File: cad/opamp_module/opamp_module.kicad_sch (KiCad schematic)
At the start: 28 parts, among them J1 Conn_02x04_Odd_Even, U1 OPA2325, U2 REF3433IDBVR

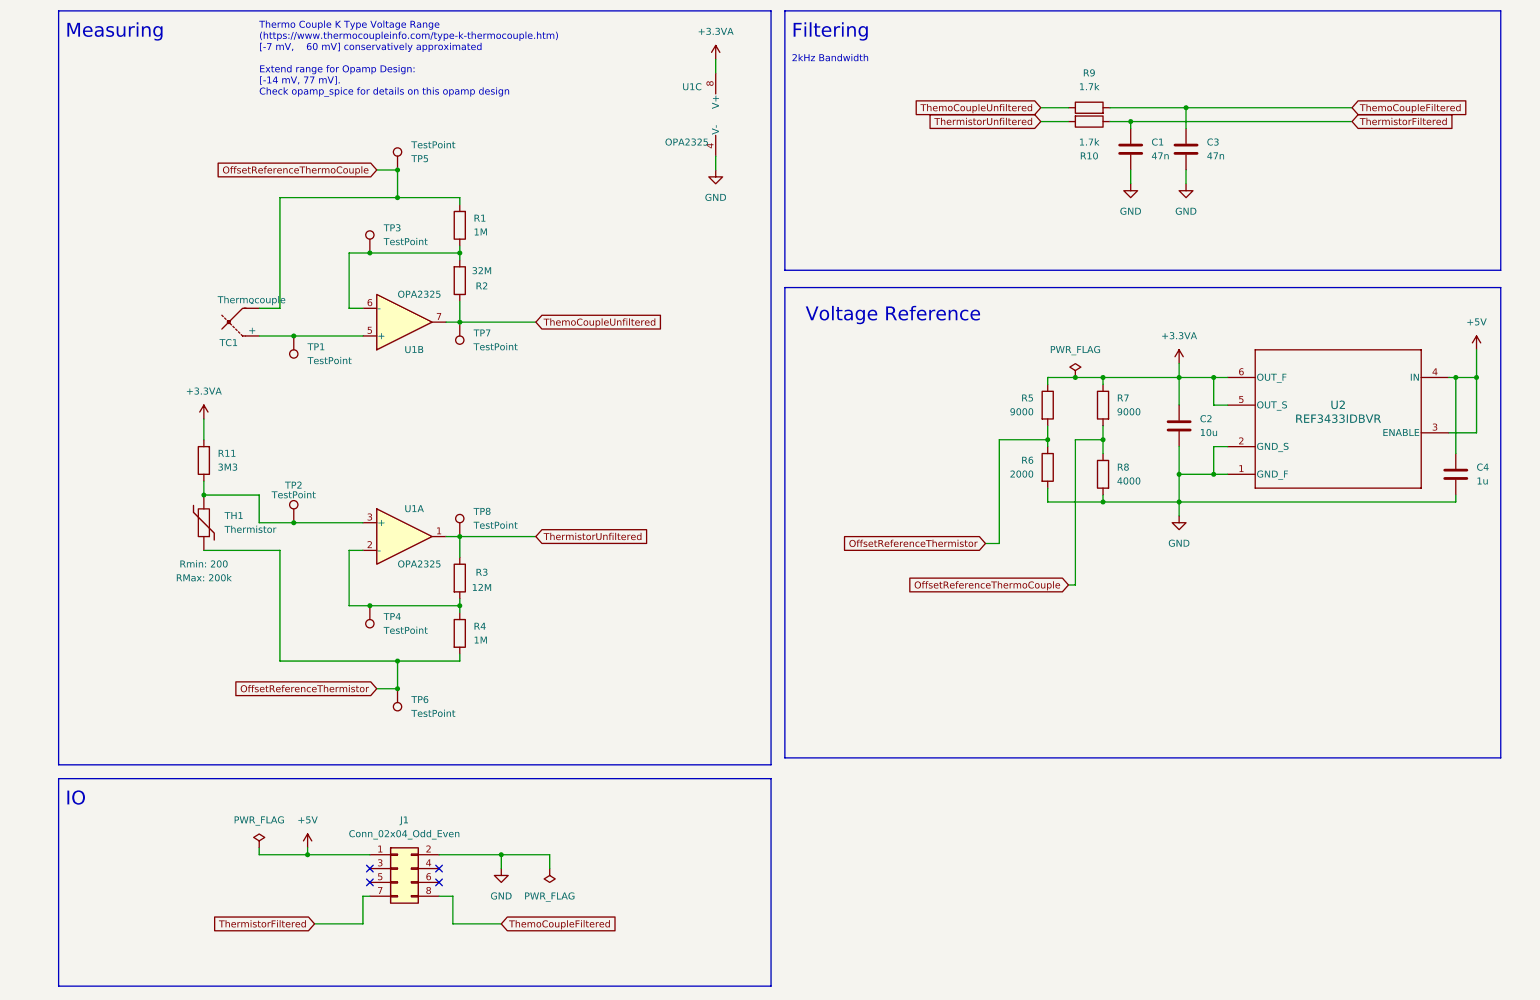
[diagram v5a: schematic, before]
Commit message: Spice simulations and switching to two TC's per module
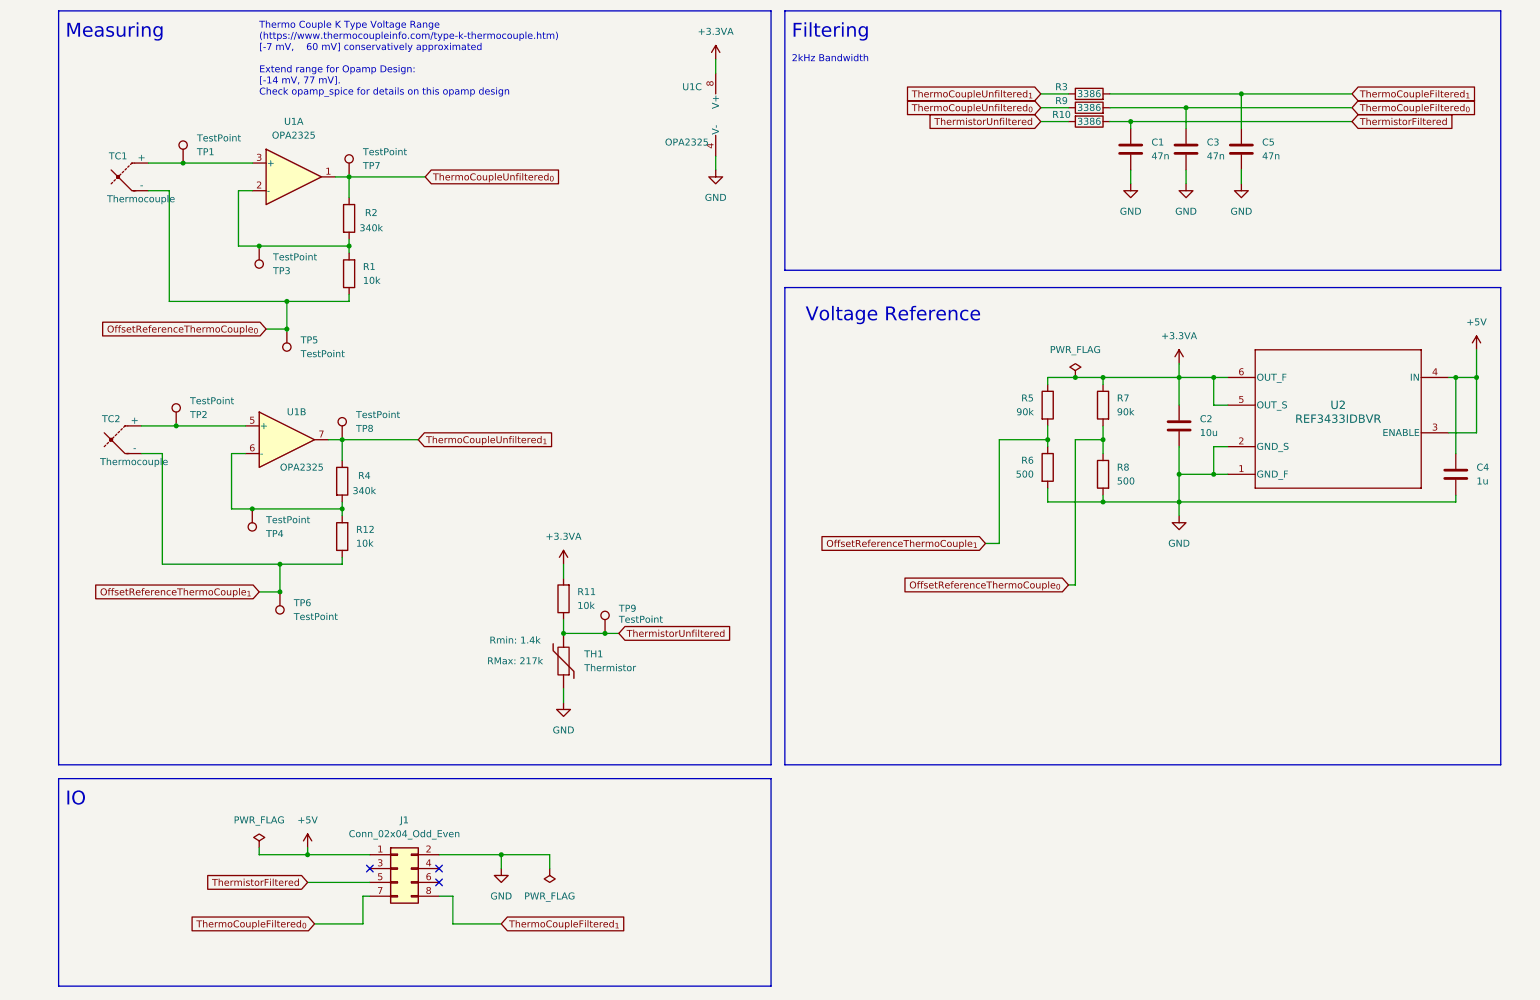
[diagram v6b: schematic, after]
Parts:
- added C5: 47n, Capacitor_SMD:C_0805_2012Metric_Pad1.18x1.45mm_HandSolder, symbol Device:C
- added R12: 10k, Resistor_SMD:R_0805_2012Metric_Pad1.20x1.40mm_HandSolder, symbol Device:R
- added TC2: Thermocouple, Connector_PinHeader_2.54mm:PinHeader_1x02_P2.54mm_Vertical, symbol Device:Thermocouple
- added TP9: TestPoint, TestPoint:TestPoint_Pad_D2.0mm, symbol Connector:TestPoint
- R1: value 1M -> 10k
- R10, R9: value 1.7k -> 3386
- R11: value 3M3 -> 10k
- R2: value 32M -> 340k
- R3: value 12M -> 3386
- R4: value 1M -> 340k
- R5, R7: value 9000 -> 90k
- R6: value 2000 -> 500
- R8: value 4000 -> 500
- TH1: RMax 200k -> 217k; Rmin 200 -> 1.4k
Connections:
- net GND: now also TH1.1, C5.2
- net ThermistorFiltered: now also J1.5 (Pin_5); no longer J1.7 (Pin_7)
- net ThermistorUnfiltered: now also R11.1, TH1.2, TP9.1; no longer R3.1, TP8.1, U1.1
- net at TC1.1 (+), TP1.1: now also U1.3 (+); no longer U1.5 (+)
- net at R2.2, TP3.1: now also R1.2, U1.2 (-); no longer R1.1, U1.6 (-)
- net OffsetReferenceThermistor renamed OffsetReferenceThermoCouple_{1}
- net OffsetReferenceThermoCouple_{1}: now also R12.1, TC2.2 (-); no longer R4.2, TH1.1
- net OffsetReferenceThermoCouple renamed OffsetReferenceThermoCouple_{0}
- net OffsetReferenceThermoCouple_{0}: now also R1.1; no longer R1.2
- net ThemoCoupleFiltered renamed ThermoCoupleFiltered_{0}
- net ThermoCoupleFiltered_{0}: now also J1.7 (Pin_7); no longer J1.8 (Pin_8)
- net ThemoCoupleUnfiltered renamed ThermoCoupleUnfiltered_{0}
- net ThermoCoupleUnfiltered_{0}: now also U1.1; no longer U1.7
- new net: R12.2, R4.2, TP4.1, U1.6 (-)
- new net: TC2.1 (+), TP2.1, U1.5 (+)
- new net ThermoCoupleFiltered_{1}: C5.1, J1.8 (Pin_8), R3.2
- new net ThermoCoupleUnfiltered_{1}: R3.1, R4.1, TP8.1, U1.7
- no-connect marks 4 -> 3
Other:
- moved on the sheet: R1, R11, R2, TC1, TH1, TP1, TP3, TP5, TP7, U1B

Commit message: Ordered
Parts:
- R10, R3, R9: value 3386 -> 3.4k
- R5, R7: value 90k -> 90.9k
- R6, R8: value 500 -> 499
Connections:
- net GND: now also R1.1, R12.1
- net OffsetReferenceThermoCouple_{0}: no longer R1.1
- net OffsetReferenceThermoCouple_{1}: no longer R12.1
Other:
- moved on the sheet: R6
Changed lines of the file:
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@@
 	)
 	(junction
-		(at 57.15 68.58)
-		(diameter 0)
-		(color 0 0 0 0)
-	)
-	(junction
 		(at 55.88 121.92)
 		(diameter 0)
@@
 	)
 	(junction
-		(at 55.88 116.84)
-		(diameter 0)
-		(color 0 0 0 0)
-	)
-	(junction
 		(at 60.96 170.18)
 		(diameter 0)
@@
 	(wire
 		(pts
-			(xy 68.58 68.58) (xy 68.58 67.31)
+			(xy 50.8 106.68) (xy 46.99 106.68)
 		)
 		(stroke
@@
 	(wire
 		(pts
-			(xy 50.8 106.68) (xy 46.99 106.68)
+			(xy 35.56 68.58) (xy 57.15 68.58)
 		)
 		(stroke
@@
 	(wire
 		(pts
-			(xy 35.56 68.58) (xy 57.15 68.58)
+			(xy 68.58 67.31) (xy 68.58 71.12)
 		)
 		(stroke
@@
 	(wire
 		(pts
-			(xy 57.15 68.58) (xy 68.58 68.58)
-		)
-		(stroke
-			(width 0)
-			(type default)
-		)
-	)
-	(wire
-		(pts
 			(xy 275.59 92.71) (xy 270.51 92.71)
 		)
@@
 	(wire
 		(pts
-			(xy 55.88 116.84) (xy 67.31 116.84)
-		)
-		(stroke
-			(width 0)
-			(type default)
-		)
-	)
-	(wire
-		(pts
 			(xy 96.52 170.18) (xy 96.52 172.72)
 		)
@@
 	(wire
 		(pts
-			(xy 196.85 105.41) (xy 196.85 102.87)
+			(xy 196.85 105.41) (xy 196.85 104.14)
 		)
 		(stroke
@@
 	(wire
 		(pts
-			(xy 67.31 116.84) (xy 67.31 115.57)
+			(xy 67.31 115.57) (xy 67.31 119.38)
 		)
 		(stroke
@@
 	(wire
 		(pts
-			(xy 196.85 93.98) (xy 196.85 95.25)
+			(xy 196.85 93.98) (xy 196.85 96.52)
 		)
 		(stroke
@@
 	(symbol
 		(lib_id "power:GND")
+		(at 67.31 119.38 0)
+		(unit 1)
+		(exclude_from_sim no)
+		(in_bom yes)
+		(on_board yes)
+		(dnp no)
+		(fields_autoplaced yes)
+		(property "Reference" "#PWR014"
+			(at 67.31 125.73 0)
+			(effects
+				(font
+					(size 1.27 1.27)
+				)
+				(hide yes)
+			)
+		)
+		(property "Value" "GND"
+			(at 67.31 124.46 0)
+			(effects
+				(font
+					(size 1.27 1.27)
+				)
+			)
+		)
+		(property "Footprint" ""
+			(at 67.31 119.38 0)
+			(effects
+				(font
+					(size 1.27 1.27)
+				)
+				(hide yes)
+			)
+		)
+		(property "Datasheet" ""
+			(at 67.31 119.38 0)
+			(effects
+				(font
+					(size 1.27 1.27)
+				)
+				(hide yes)
+			)
+		)
+		(property "Description" "Power symbol creates a global label with name \"GND\" , ground"
+			(at 67.31 119.38 0)
+			(effects
+				(font
+					(size 1.27 1.27)
+				)
+				(hide yes)
+			)
+		)
+		(pin "1"
+		)
+		(instances
+			(project "opamp_module"
+				(path "/d4d6d439-2cda-48a0-9eae-d76ddb675c53"
+					(reference "#PWR014")
+					(unit 1)
+				)
+			)
+		)
+	)
+	(symbol
+		(lib_id "power:GND")
 		(at 232.41 46.99 0)
 		(unit 1)
@@
 			)
 		)
-		(property "Value" "3386"
+		(property "Value" "3.4k"
 			(at 204.47 30.48 90)
 			(effects
@@
 			)
 		)
-		(property "Value" "3386"
+		(property "Value" "3.4k"
 			(at 204.47 35.56 90)
 			(effects
@@
 			)
 		)
-		(property "Value" "3386"
+		(property "Value" "3.4k"
 			(at 204.47 33.02 90)
 			(effects
@@
 			)
 		)
-		(property "Value" "90k"
+		(property "Value" "90.9k"
 			(at 209.55 88.8999 0)
 			(effects
@@
 	)
 	(symbol
+		(lib_id "power:GND")
+		(at 68.58 71.12 0)
+		(unit 1)
+		(exclude_from_sim no)
+		(in_bom yes)
+		(on_board yes)
+		(dnp no)
+		(fields_autoplaced yes)
+		(property "Reference" "#PWR013"
+			(at 68.58 77.47 0)
+			(effects
+				(font
+					(size 1.27 1.27)
+				)
+				(hide yes)
+			)
+		)
+		(property "Value" "GND"
+			(at 68.58 76.2 0)
+			(effects
+				(font
+					(size 1.27 1.27)
+				)
+			)
+		)
+		(property "Footprint" ""
+			(at 68.58 71.12 0)
+			(effects
+				(font
+					(size 1.27 1.27)
+				)
+				(hide yes)
+			)
+		)
+		(property "Datasheet" ""
+			(at 68.58 71.12 0)
+			(effects
+				(font
+					(size 1.27 1.27)
+				)
+				(hide yes)
+			)
+		)
+		(property "Description" "Power symbol creates a global label with name \"GND\" , ground"
+			(at 68.58 71.12 0)
+			(effects
+				(font
+					(size 1.27 1.27)
+				)
+				(hide yes)
+			)
+		)
+		(pin "1"
+		)
+		(instances
+			(project ""
+				(path "/d4d6d439-2cda-48a0-9eae-d76ddb675c53"
+					(reference "#PWR013")
+					(unit 1)
+				)
+			)
+		)
+	)
+	(symbol
 		(lib_id "Device:C")
 		(at 271.78 100.33 0)
@@
 			)
 		)
-		(property "Value" "90k"
+		(property "Value" "90.9k"
 			(at 194.31 88.8999 0)
 			(effects
@@
 			)
 		)
-		(property "Value" "500"
+		(property "Value" "499"
 			(at 209.55 101.5999 0)
 			(effects
@@
 	(symbol
 		(lib_id "Device:R")
-		(at 196.85 99.06 0)
+		(at 196.85 100.33 0)
 		(unit 1)
 		(exclude_from_sim no)
@@
 		(dnp no)
 		(property "Reference" "R6"
-			(at 194.31 97.7899 0)
+			(at 194.31 99.0599 0)
 			(effects
 				(font
@@
 			)
 		)
-		(property "Value" "500"
-			(at 194.31 100.3299 0)
+		(property "Value" "499"
+			(at 194.31 101.5999 0)
 			(effects
 				(font
@@
 		)
 		(property "Footprint" "Resistor_SMD:R_0805_2012Metric_Pad1.20x1.40mm_HandSolder"
-			(at 195.072 99.06 90)
+			(at 195.072 100.33 90)
 			(effects
 				(font
@@
 		)
 		(property "Datasheet" "~"
-			(at 196.85 99.06 0)
+			(at 196.85 100.33 0)
 			(effects
 				(font
@@
 		)
 		(property "Description" "Resistor"
-			(at 196.85 99.06 0)
+			(at 196.85 100.33 0)
 			(effects
 				(font
